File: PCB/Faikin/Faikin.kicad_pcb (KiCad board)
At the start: 2 copper layers, 70 x 70 mm, 28 parts, among them J1 1x5, J2 Shelly, J3 USB-PROG, Q1 BSS138PS, U3 MD8942, U4 ESP32-S3-MINI-1

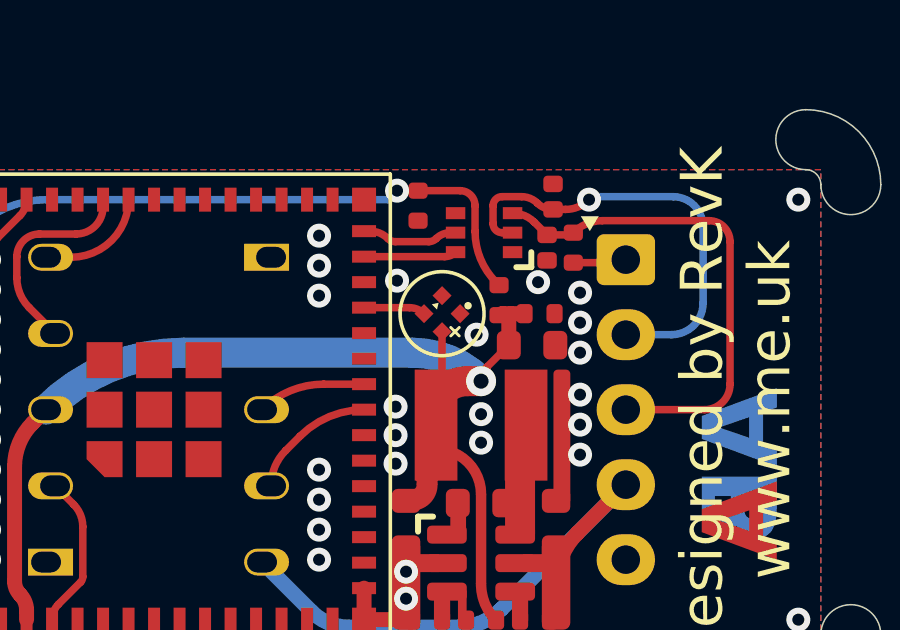
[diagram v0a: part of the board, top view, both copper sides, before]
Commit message: Bigger pads
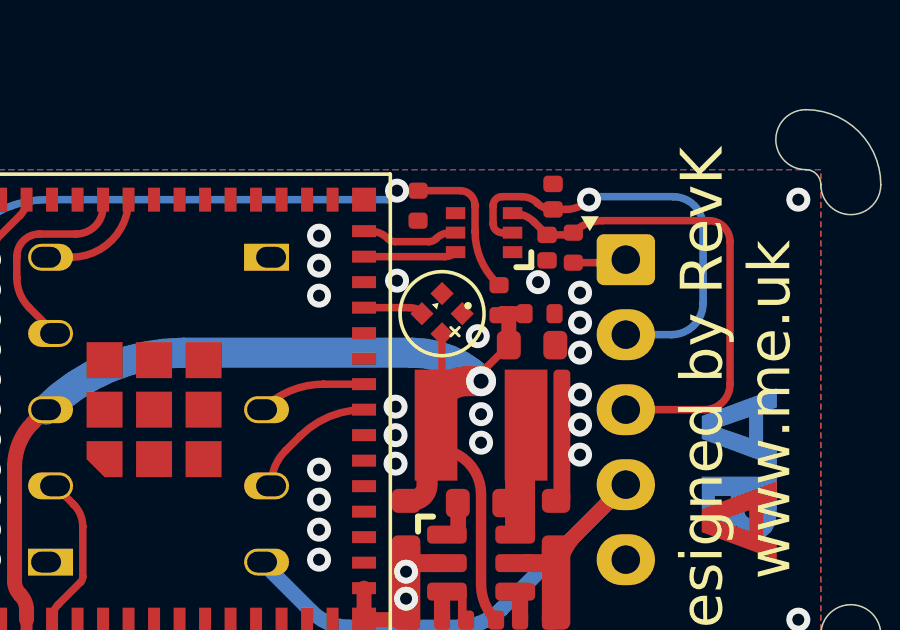
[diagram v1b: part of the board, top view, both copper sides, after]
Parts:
- D1: footprint RevK:SMD1010 -> RevK:SMD1010+

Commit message: KiCad 8.0
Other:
- board text removed: "70x70mm panel"

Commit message: Tweak
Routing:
- net DC: track 19.0 -> 17.0 mm

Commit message: Tweak
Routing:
- net GND: vias 37 -> 38

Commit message: Library update
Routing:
- net GND: vias 38 -> 37

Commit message: Tweaks
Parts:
- moved R3 0.59 mm to (146.7, 60.8), turned to 180 degrees
- moved D1 0.15 mm to (144.8, 61.8), turned to 180 degrees
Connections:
- U4 pad 25: unconnected-(U4-GPIO21-Pad25) -> GND
- U4 pad 28: unconnected-(U4-GPIO33-Pad28) -> GND
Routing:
- net +3.3V: track 31.8 -> 36.1 mm
- net GND: track 5.05 -> 8.85 mm, vias 37 -> 36

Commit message: Library update
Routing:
- net GND: vias 36 -> 37
